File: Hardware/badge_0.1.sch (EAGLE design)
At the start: 59 parts, among them CON1 PH_2, IC1 CP2102, SW1 MK12C02, SW2 MK12C02, U1 SMBT2222A, U2 SMBT2222A, U4 MCP73832T-2DCI/OT

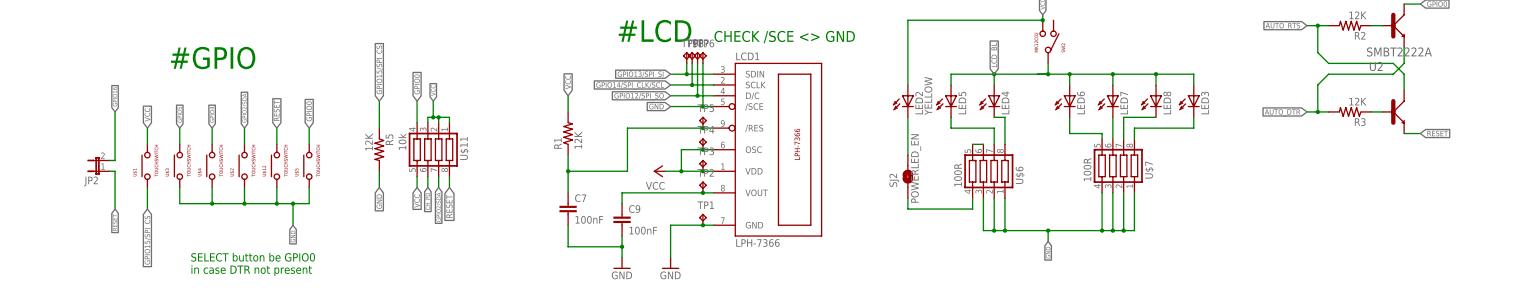
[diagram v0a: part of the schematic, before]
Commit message: Connect GPIO16 to RESET via diode to enable deep sleep.
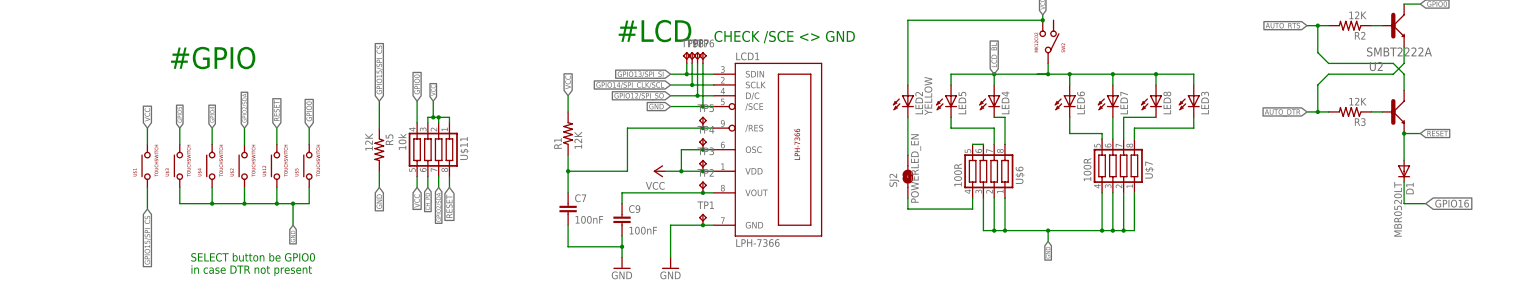
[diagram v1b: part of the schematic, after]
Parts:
- removed JP2: (no value), SparkFun-Retired:JUMPER-2SMD-NO
- added D1: MBR0520LT, diode:MBR0520LT
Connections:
- net GPIO16: now also D1.C; no longer JP2.2
- net RESET: now also D1.A; no longer JP2.1
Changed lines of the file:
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@@
 <part name="SJ2" library="SparkFun-Retired" deviceset="SOLDERJUMPER" device="TRACE" value="POWERLED_EN"/>
 <part name="U$14" library="Simplex-rlc" deviceset="RES_ARR" device="" value="1k"/>
-<part name="JP2" library="SparkFun-Retired" deviceset="JUMPER-2" device="SMD-NO"/>
 <part name="J3" library="SparkFun-Connectors" deviceset="M16" device="PTH"/>
 <part name="J4" library="SparkFun-Connectors" deviceset="M08" device=""/>
@@
 <part name="TP8" library="testpad" deviceset="TP" device="B1,27" value="TPB1,27"/>
 <part name="TP9" library="testpad" deviceset="TP" device="B1,27" value="TPB1,27"/>
+<part name="D1" library="diode" deviceset="MBR0520LT" device=""/>
 </parts>
 <sheets>
@@
 </instance>
 <instance part="U$14" gate="G$1" x="85.09" y="109.22" rot="R90"/>
-<instance part="JP2" gate="A" x="38.1" y="53.34" rot="R90"/>
 <instance part="J3" gate="G$1" x="199.39" y="149.86" rot="MR180"/>
 <instance part="J4" gate="G$1" x="344.17" y="165.1" rot="R180"/>
@@
 <instance part="TP8" gate="G$1" x="177.8" y="81.28"/>
 <instance part="TP9" gate="G$1" x="176.53" y="81.28"/>
+<instance part="D1" gate="G$1" x="345.44" y="53.34" rot="R270"/>
 </instances>
 <busses>
@@
 </segment>
 <segment>
-<wire x1="41.91" y1="53.34" x2="41.91" y2="44.45" width="0.1524" layer="91"/>
-<pinref part="JP2" gate="A" pin="1"/>
-<wire x1="40.64" y1="53.34" x2="41.91" y2="53.34" width="0.1524" layer="91"/>
-<label x="41.91" y="44.45" size="1.016" layer="95" rot="R270" xref="yes"/>
-</segment>
-<segment>
 <pinref part="J3" gate="G$1" pin="1"/>
 <wire x1="213.36" y1="170.18" x2="209.55" y2="170.18" width="0.1524" layer="91"/>
@@
 <wire x1="345.44" y1="62.23" x2="349.25" y2="62.23" width="0.1524" layer="91"/>
 <label x="349.25" y="62.23" size="1.27" layer="95" xref="yes"/>
+<wire x1="345.44" y1="62.23" x2="345.44" y2="55.88" width="0.1524" layer="91"/>
+<pinref part="D1" gate="G$1" pin="A"/>
+<junction x="345.44" y="62.23"/>
 </segment>
 </net>
@@
 </segment>
 <segment>
-<wire x1="41.91" y1="67.31" x2="41.91" y2="55.88" width="0.1524" layer="91"/>
-<label x="41.91" y="67.31" size="1.016" layer="95" rot="R90" xref="yes"/>
-<pinref part="JP2" gate="A" pin="2"/>
-<wire x1="40.64" y1="55.88" x2="41.91" y2="55.88" width="0.1524" layer="91"/>
-</segment>
-<segment>
 <wire x1="213.36" y1="147.32" x2="209.55" y2="147.32" width="0.1524" layer="91"/>
 <label x="213.36" y="147.32" size="1.016" layer="95" xref="yes"/>
 <pinref part="J3" gate="G$1" pin="10"/>
 </segment>
-</net>
+<segment>
+<pinref part="D1" gate="G$1" pin="C"/>
+<wire x1="345.44" y1="50.8" x2="345.44" y2="45.72" width="0.1524" layer="91"/>
+<wire x1="345.44" y1="45.72" x2="350.52" y2="45.72" width="0.1524" layer="91"/>
+<label x="350.52" y="45.72" size="1.778" layer="95" xref="yes"/>
+</segment>
+</net>

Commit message: Added auto-switch between battery & USB power, just like Huzzah. Removed the need for switch SW1. Since lipo charger output is now the same as regulator input, and C2 & C4 were next to each other, C2 was removed. The empty space allowed battery connector to be moved up, away from the UP button.
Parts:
- removed C2: 10uF, SparkFun-Capacitors:1UF-25V-10%(0805)"
- removed SW1: MK12C02, badge:MK12C02
- added D2: MBR0520LT, diode:MBR0520LT
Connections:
- removed net VREG_IN: C4.1, SW1.P$1, U$9.VIN, U$9.~SHDN
- net 5V: now also C4.1, D2.C, U$9.VIN, U$9.~SHDN; no longer C2.1, SW1.P$2
- net GND: no longer C2.2
- net VBAT: now also D2.A; no longer SW1.P$3
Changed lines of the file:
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@@
 <part name="U$4" library="badge" deviceset="TOUCHSWITCH" device=""/>
 <part name="U$5" library="badge" deviceset="TOUCHSWITCH" device=""/>
-<part name="SW1" library="badge" deviceset="MK12C02" device=""/>
 <part name="U4" library="Microchip_By_element14_Batch_1" deviceset="MCP73832T-2DCI/OT" device=""/>
 <part name="U6" library="esp8266modules" deviceset="ESP12E" device="SMD"/>
@@
 <part name="LED2" library="led" deviceset="LED" device="SML0805" value="YELLOW"/>
 <part name="C1" library="SparkFun-Capacitors" deviceset="1UF-25V-10%(0805)" device="&quot;" value="10uF"/>
-<part name="C2" library="SparkFun-Capacitors" deviceset="1UF-25V-10%(0805)" device="&quot;" value="10uF"/>
 <part name="CON1" library="badge" deviceset="PH_2" device=""/>
 <part name="IC1" library="silabs" deviceset="CP210*" device="" technology="2"/>
@@
 <part name="TP9" library="testpad" deviceset="TP" device="B1,27" value="TPB1,27"/>
 <part name="D1" library="diode" deviceset="MBR0520LT" device=""/>
+<part name="D2" library="diode" deviceset="MBR0520LT" device=""/>
 </parts>
 <sheets>
@@
 <instance part="U$4" gate="G$1" x="64.77" y="54.61" rot="R90"/>
 <instance part="U$5" gate="G$1" x="87.63" y="54.61" rot="R90"/>
-<instance part="SW1" gate="G$1" x="241.3" y="227.33" rot="MR0"/>
 <instance part="U4" gate="A" x="63.5" y="130.81"/>
 <instance part="U6" gate="G$1" x="278.13" y="160.02"/>
@@
 <instance part="LED2" gate="G$1" x="228.6" y="71.12"/>
 <instance part="C1" gate="G$1" x="43.18" y="118.11"/>
-<instance part="C2" gate="G$1" x="99.06" y="120.65"/>
 <instance part="CON1" gate="G$1" x="224.79" y="214.63" rot="MR0"/>
 <instance part="IC1" gate="G$1" x="81.28" y="213.36"/>
@@
 <instance part="TP9" gate="G$1" x="176.53" y="81.28"/>
 <instance part="D1" gate="G$1" x="345.44" y="53.34" rot="R270"/>
+<instance part="D2" gate="G$1" x="239.014" y="224.79"/>
 </instances>
 <busses>
@@
 <wire x1="99.06" y1="110.49" x2="99.06" y2="107.95" width="0.1524" layer="91"/>
 <label x="99.06" y="107.95" size="1.016" layer="95" rot="R270" xref="yes"/>
-<pinref part="C2" gate="G$1" pin="2"/>
-<wire x1="99.06" y1="118.11" x2="99.06" y2="110.49" width="0.1524" layer="91"/>
-<junction x="99.06" y="110.49"/>
 <wire x1="95.25" y1="110.49" x2="99.06" y2="110.49" width="0.1524" layer="91"/>
-<junction x="99.06" y="110.49"/>
 <wire x1="95.25" y1="101.6" x2="95.25" y2="110.49" width="0.1524" layer="91"/>
 <pinref part="U$14" gate="G$1" pin="3"/>
@@
 </segment>
 </net>
-<net name="VREG_IN" class="0">
-<segment>
-<pinref part="SW1" gate="G$1" pin="P$1"/>
-<pinref part="C4" gate="G$1" pin="1"/>
-<wire x1="247.65" y1="227.33" x2="246.38" y2="227.33" width="0.1524" layer="91"/>
-<wire x1="237.49" y1="217.17" x2="237.49" y2="219.71" width="0.1524" layer="91"/>
-<wire x1="237.49" y1="219.71" x2="247.65" y2="219.71" width="0.1524" layer="91"/>
-<wire x1="247.65" y1="219.71" x2="247.65" y2="224.79" width="0.1524" layer="91"/>
-<pinref part="U$9" gate="A" pin="VIN"/>
-<wire x1="247.65" y1="224.79" x2="247.65" y2="227.33" width="0.1524" layer="91"/>
-<wire x1="247.65" y1="224.79" x2="262.89" y2="224.79" width="0.1524" layer="91"/>
-<junction x="247.65" y="224.79"/>
-<junction x="247.65" y="219.71"/>
-<pinref part="U$9" gate="A" pin="~SHDN"/>
-<wire x1="247.65" y1="219.71" x2="262.89" y2="219.71" width="0.1524" layer="91"/>
-<label x="247.65" y="222.25" size="1.27" layer="95" xref="yes"/>
-</segment>
-</net>
 <net name="D-" class="0">
 <segment>
@@
 <segment>
 <label x="232.41" y="224.79" size="1.016" layer="95" rot="R180" xref="yes"/>
-<pinref part="SW1" gate="G$1" pin="P$3"/>
-<wire x1="236.22" y1="226.06" x2="232.41" y2="226.06" width="0.1524" layer="91"/>
-<wire x1="232.41" y1="217.17" x2="232.41" y2="226.06" width="0.1524" layer="91"/>
+<wire x1="236.474" y1="224.79" x2="232.41" y2="224.79" width="0.1524" layer="91"/>
+<wire x1="232.41" y1="217.17" x2="232.41" y2="224.79" width="0.1524" layer="91"/>
 <pinref part="CON1" gate="G$1" pin="P$1"/>
 <wire x1="229.87" y1="217.17" x2="232.41" y2="217.17" width="0.1524" layer="91"/>
+<pinref part="D2" gate="G$1" pin="A"/>
 </segment>
 </net>
@@
 <net name="5V" class="0">
 <segment>
-<wire x1="232.41" y1="228.6" x2="232.41" y2="232.41" width="0.1524" layer="91"/>
-<label x="232.41" y="232.41" size="1.016" layer="95" rot="R90" xref="yes"/>
-<pinref part="SW1" gate="G$1" pin="P$2"/>
-<wire x1="236.22" y1="228.6" x2="232.41" y2="228.6" width="0.1524" layer="91"/>
-</segment>
-<segment>
 <pinref part="JP1" gate="A" pin="4"/>
 <wire x1="60.96" y1="182.88" x2="71.12" y2="182.88" width="0.1524" layer="91"/>
@@
 <segment>
 <pinref part="U4" gate="A" pin="VDD"/>
-<pinref part="C2" gate="G$1" pin="1"/>
 <wire x1="81.28" y1="128.27" x2="83.82" y2="128.27" width="0.1524" layer="91"/>
 <wire x1="83.82" y1="128.27" x2="99.06" y2="128.27" width="0.1524" layer="91"/>
-<wire x1="99.06" y1="128.27" x2="99.06" y2="125.73" width="0.1524" layer="91"/>
 <label x="99.06" y="128.27" size="1.27" layer="95" xref="yes"/>
 <pinref part="LED1" gate="G$1" pin="A"/>
@@
 <junction x="83.82" y="128.27"/>
 </segment>
-</net>
+<segment>
+<pinref part="C4" gate="G$1" pin="1"/>
+<wire x1="237.49" y1="217.17" x2="237.49" y2="219.71" width="0.1524" layer="91"/>
+<wire x1="237.49" y1="219.71" x2="247.65" y2="219.71" width="0.1524" layer="91"/>
+<wire x1="247.65" y1="219.71" x2="247.65" y2="224.79" width="0.1524" layer="91"/>
+<junction x="247.65" y="219.71"/>
+<pinref part="U$9" gate="A" pin="~SHDN"/>
+<wire x1="247.65" y1="219.71" x2="262.89" y2="219.71" width="0.1524" layer="91"/>
+<label x="247.65" y="229.616" size="1.016" layer="95" rot="R90" xref="yes"/>
+<wire x1="247.65" y1="224.79" x2="247.65" y2="229.616" width="0.1524" layer="91"/>
+<pinref part="U$9" gate="A" pin="VIN"/>
+<wire x1="241.554" y1="224.79" x2="247.65" y2="224.79" width="0.1524" layer="91"/>
+<pinref part="D2" gate="G$1" pin="C"/>
+<junction x="247.65" y="224.79"/>
+<wire x1="247.65" y1="224.79" x2="262.89" y2="224.79" width="0.1524" layer="91"/>
+</segment>
+</net>

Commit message: Fixed transistor layout; Repositioned LCD caps; added 10uF cap to LCD for Brownouts; Increased width of custom layouts; Unbridged 5v; Changed name to FeTChX; ref C; Encoded names; Changed XCTF logo width; Converted Names to pads
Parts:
- added C2: 10uF, SparkFun-Capacitors:1UF-25V-10%(0805)"
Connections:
- removed net N$17: C7.1, LCD1./RES, R1.1, TP5.TP
- net AUTO_RTS: now also U2.E; no longer U2.C
- net GND: now also C2.2
- net RESET: now also C7.1, LCD1./RES, R1.1, TP5.TP, U2.C; no longer U2.E
- net VCC: now also C2.1
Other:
- moved on the sheet: U2
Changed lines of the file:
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@@
 <setting verticaltext="up"/>
 </settings>
-<grid distance="0.1" unitdist="inch" unit="inch" style="lines" multiple="1" display="no" altdistance="0.01" altunitdist="inch" altunit="inch"/>
+<grid distance="0.05" unitdist="inch" unit="inch" style="lines" multiple="1" display="no" altdistance="0.01" altunitdist="inch" altunit="inch"/>
 <layers>
 <layer number="1" name="Top" color="4" fill="1" visible="no" active="no"/>
@@
 <part name="D1" library="diode" deviceset="MBR0520LT" device=""/>
 <part name="D2" library="diode" deviceset="MBR0520LT" device=""/>
+<part name="C2" library="SparkFun-Capacitors" deviceset="1UF-25V-10%(0805)" device="&quot;" value="10uF"/>
 </parts>
 <sheets>
@@
 <instance part="R1" gate="G$1" x="148.59" y="62.23" rot="R90"/>
 <instance part="U1" gate="A" x="342.9" y="87.63"/>
-<instance part="U2" gate="A" x="342.9" y="67.31"/>
+<instance part="U2" gate="A" x="342.9" y="67.31" rot="MR180"/>
 <instance part="R2" gate="G$1" x="332.74" y="87.63" rot="R180"/>
 <instance part="R3" gate="G$1" x="332.74" y="67.31" rot="R180"/>
@@
 <instance part="D1" gate="G$1" x="345.44" y="53.34" rot="R270"/>
 <instance part="D2" gate="G$1" x="239.014" y="224.79"/>
+<instance part="C2" gate="G$1" x="316.23" y="214.63"/>
 </instances>
 <busses>
@@
 <pinref part="U$9" gate="A" pin="VOUT"/>
 <wire x1="298.45" y1="224.79" x2="306.07" y2="224.79" width="0.1524" layer="91"/>
-<wire x1="306.07" y1="224.79" x2="321.31" y2="224.79" width="0.1524" layer="91"/>
+<wire x1="306.07" y1="224.79" x2="316.23" y2="224.79" width="0.1524" layer="91"/>
 <junction x="306.07" y="224.79"/>
+<wire x1="316.23" y1="224.79" x2="321.31" y2="224.79" width="0.1524" layer="91"/>
 <wire x1="321.31" y1="224.79" x2="326.39" y2="224.79" width="0.1524" layer="91"/>
 <junction x="321.31" y="224.79"/>
@@
 <pinref part="P+5" gate="VCC" pin="VCC"/>
 <wire x1="321.31" y1="229.87" x2="321.31" y2="224.79" width="0.1524" layer="91"/>
+<pinref part="C2" gate="G$1" pin="1"/>
+<wire x1="316.23" y1="224.79" x2="316.23" y2="219.71" width="0.1524" layer="91"/>
+<junction x="316.23" y="224.79"/>
 </segment>
 <segment>
@@
 <wire x1="229.87" y1="214.63" x2="232.41" y2="214.63" width="0.1524" layer="91"/>
 <wire x1="232.41" y1="214.63" x2="232.41" y2="199.39" width="0.1524" layer="91"/>
+<pinref part="C2" gate="G$1" pin="2"/>
+<wire x1="306.07" y1="199.39" x2="316.23" y2="199.39" width="0.1524" layer="91"/>
+<wire x1="316.23" y1="199.39" x2="316.23" y2="212.09" width="0.1524" layer="91"/>
+<junction x="306.07" y="199.39"/>
 </segment>
 <segment>
@@
 <label x="120.65" y="49.53" size="1.4224" layer="95" rot="R270" xref="yes"/>
 <pinref part="U$11" gate="G$1" pin="8"/>
-<wire x1="120.65" y1="52.07" x2="120.65" y2="49.53" width="0.1524" layer="91"/>
+<wire x1="120.65" y1="52.07" x2="120.65" y2="50.8" width="0.1524" layer="91"/>
+<pinref part="R1" gate="G$1" pin="1"/>
+<pinref part="C7" gate="G$1" pin="1"/>
+<wire x1="120.65" y1="50.8" x2="120.65" y2="49.53" width="0.1524" layer="91"/>
+<wire x1="148.59" y1="57.15" x2="148.59" y2="53.34" width="0.1524" layer="91"/>
+<wire x1="148.59" y1="53.34" x2="148.59" y2="50.8" width="0.1524" layer="91"/>
+<wire x1="148.59" y1="50.8" x2="148.59" y2="48.26" width="0.1524" layer="91"/>
+<wire x1="148.59" y1="53.34" x2="162.56" y2="53.34" width="0.1524" layer="91"/>
+<wire x1="162.56" y1="53.34" x2="162.56" y2="63.5" width="0.1524" layer="91"/>
+<junction x="148.59" y="53.34"/>
+<pinref part="LCD1" gate="G$1" pin="/RES"/>
+<wire x1="182.88" y1="63.5" x2="180.34" y2="63.5" width="0.1524" layer="91"/>
+<pinref part="TP5" gate="G$1" pin="TP"/>
+<wire x1="180.34" y1="63.5" x2="162.56" y2="63.5" width="0.1524" layer="91"/>
+<junction x="180.34" y="63.5"/>
+<wire x1="120.65" y1="50.8" x2="148.59" y2="50.8" width="0.1524" layer="91"/>
+<junction x="120.65" y="50.8"/>
+<junction x="148.59" y="50.8"/>
 </segment>
 <segment>
@@
 </segment>
 <segment>
-<pinref part="U2" gate="A" pin="E"/>
-<wire x1="345.44" y1="62.23" x2="349.25" y2="62.23" width="0.1524" layer="91"/>
 <label x="349.25" y="62.23" size="1.27" layer="95" xref="yes"/>
-<wire x1="345.44" y1="62.23" x2="345.44" y2="55.88" width="0.1524" layer="91"/>
+<wire x1="347.98" y1="62.23" x2="349.25" y2="62.23" width="0.1524" layer="91"/>
 <pinref part="D1" gate="G$1" pin="A"/>
-<junction x="345.44" y="62.23"/>
+<wire x1="345.44" y1="59.69" x2="345.44" y2="55.88" width="0.1524" layer="91"/>
+<wire x1="345.44" y1="59.69" x2="347.98" y2="59.69" width="0.1524" layer="91"/>
+<wire x1="347.98" y1="59.69" x2="347.98" y2="62.23" width="0.1524" layer="91"/>
+<pinref part="U2" gate="A" pin="C"/>
+<wire x1="345.44" y1="62.23" x2="345.44" y2="59.69" width="0.1524" layer="91"/>
+<junction x="345.44" y="59.69"/>
 </segment>
 </net>
@@
 <pinref part="R2" gate="G$1" pin="2"/>
 <wire x1="322.58" y1="87.63" x2="325.12" y2="87.63" width="0.1524" layer="91"/>
-<pinref part="U2" gate="A" pin="C"/>
 <wire x1="325.12" y1="87.63" x2="327.66" y2="87.63" width="0.1524" layer="91"/>
-<wire x1="345.44" y1="72.39" x2="345.44" y2="76.2" width="0.1524" layer="91"/>
 <wire x1="345.44" y1="76.2" x2="342.9" y2="78.74" width="0.1524" layer="91"/>
 <wire x1="342.9" y1="78.74" x2="327.66" y2="78.74" width="0.1524" layer="91"/>
@@
 <junction x="325.12" y="87.63"/>
 <label x="322.58" y="87.63" size="1.27" layer="95" rot="R180" xref="yes"/>
+<pinref part="U2" gate="A" pin="E"/>
+<wire x1="345.44" y1="72.39" x2="345.44" y2="76.2" width="0.1524" layer="91"/>
 </segment>
 </net>
@@
 </segment>
 </net>
-<net name="N$17" class="0">
-<segment>
-<pinref part="R1" gate="G$1" pin="1"/>
-<pinref part="C7" gate="G$1" pin="1"/>
-<wire x1="148.59" y1="57.15" x2="148.59" y2="53.34" width="0.1524" layer="91"/>
-<wire x1="148.59" y1="53.34" x2="148.59" y2="48.26" width="0.1524" layer="91"/>
-<wire x1="148.59" y1="53.34" x2="162.56" y2="53.34" width="0.1524" layer="91"/>
-<wire x1="162.56" y1="53.34" x2="162.56" y2="63.5" width="0.1524" layer="91"/>
-<junction x="148.59" y="53.34"/>
-<pinref part="LCD1" gate="G$1" pin="/RES"/>
-<wire x1="182.88" y1="63.5" x2="180.34" y2="63.5" width="0.1524" layer="91"/>
-<pinref part="TP5" gate="G$1" pin="TP"/>
-<wire x1="180.34" y1="63.5" x2="162.56" y2="63.5" width="0.1524" layer="91"/>
-<junction x="180.34" y="63.5"/>
-</segment>
-</net>
 <net name="N$10" class="0">
 <segment>
@@
 </segment>
 </net>
-<net name="N$18" class="0">
-<segment>
+<net name="N$3" class="0">
+<segment>
+<pinref part="U2" gate="A" pin="B"/>
 <pinref part="R3" gate="G$1" pin="1"/>
-<pinref part="U2" gate="A" pin="B"/>
-<wire x1="337.82" y1="67.31" x2="340.36" y2="67.31" width="0.1524" layer="91"/>
-</segment>
-</net>
+<wire x1="340.36" y1="67.31" x2="337.82" y2="67.31" width="0.1524" layer="91"/>
+</segment>
+</net>
